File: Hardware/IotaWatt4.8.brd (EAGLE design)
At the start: 87 x 67.9 mm, 53 parts

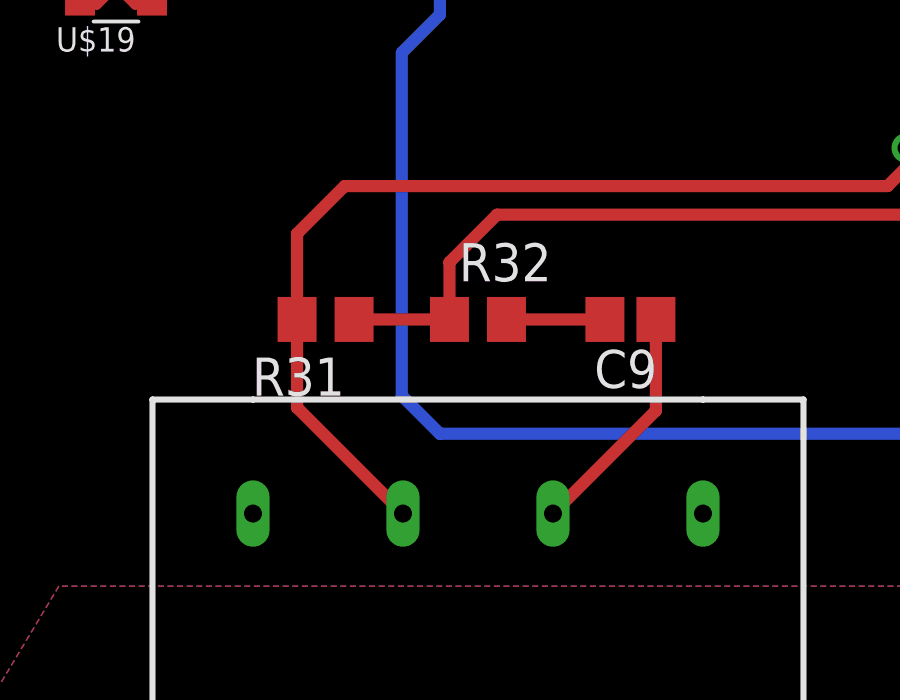
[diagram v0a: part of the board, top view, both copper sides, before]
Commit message: Revert "beginning to add a 2.2" TFT display"
This reverts commit 5a3055f75d7c66bfc0e3a1cc9d4d5180e17e1807.
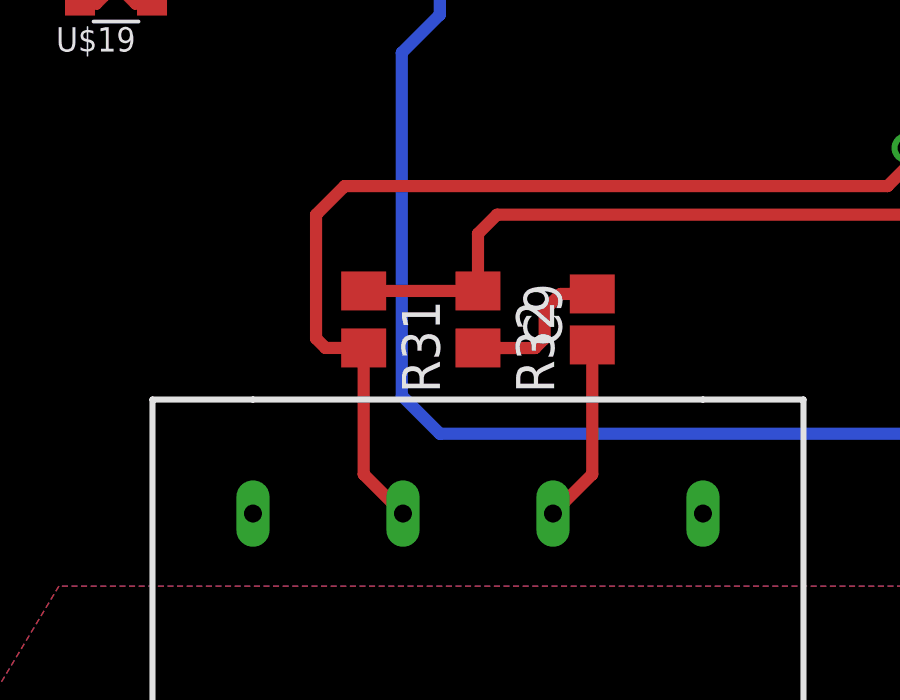
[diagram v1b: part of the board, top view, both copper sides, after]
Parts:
- moved C9 1.27 mm to (39.4, 34.3), turned to 90 degrees
- moved R31 1.27 mm to (31.8, 34.3), turned to 270 degrees
- turned R32 to 270 degrees
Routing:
- net N$17: track 3.28 -> 5.12 mm
- net N$27: track 7.89 -> 6.16 mm
- net ADC10: track 49.9 -> 49.2 mm
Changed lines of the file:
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@@
 <wire x1="17.78" y1="17.78" x2="63.5" y2="17.78" width="1.27" layer="46"/>
 <wire x1="10.16" y1="13.97" x2="16.51" y2="13.97" width="1.27" layer="46"/>
-<dimension x1="35.2425" y1="4.7625" x2="20.0025" y2="4.7625" x3="27.6225" y3="11.7475" textsize="1.778" layer="16"/>
 </plain>
 <attributes>
@@
 <attribute name="OC_NEWARK" value="unknown" x="20.0025" y="4.7625" size="1.778" layer="27" font="vector" display="off"/>
 </element>
-<element name="R31" library="resistor" package="R0805" value="1K" x="30.48" y="34.29" rot="R180"/>
-<element name="C9" library="adafruit" package="C0805" value="10uF" x="40.64" y="34.29" rot="R180"/>
-<element name="R32" library="resistor" package="R0805" value="12K" x="35.56" y="34.29"/>
+<element name="R31" library="resistor" package="R0805" value="1K" x="31.75" y="34.29" rot="R270"/>
+<element name="C9" library="adafruit" package="C0805" value="10uF" x="39.37" y="34.29" rot="R90"/>
+<element name="R32" library="resistor" package="R0805" value="12K" x="35.56" y="34.29" rot="R270"/>
 </elements>
 <signals>
@@
 <contactref element="R32" pad="1"/>
 <contactref element="R31" pad="1"/>
+<wire x1="31.75" y1="35.24" x2="35.56" y2="35.24" width="0.4064" layer="1"/>
+<wire x1="35.56" y1="35.24" x2="35.56" y2="37.1475" width="0.4064" layer="1"/>
+<wire x1="35.56" y1="37.1475" x2="36.195" y2="37.7825" width="0.4064" layer="1"/>
 <wire x1="36.195" y1="37.7825" x2="63.5" y2="37.7825" width="0.4064" layer="1"/>
 <wire x1="63.5" y1="37.7825" x2="64.77" y2="39.0525" width="0.4064" layer="1"/>
@@
 <wire x1="64.295" y1="50.68" x2="64.295" y2="48.1" width="0.4064" layer="1"/>
 <wire x1="64.295" y1="48.1" x2="64.4525" y2="47.9425" width="0.4064" layer="1"/>
-<wire x1="31.43" y1="34.29" x2="34.61" y2="34.29" width="0.4064" layer="1"/>
-<wire x1="36.195" y1="37.7825" x2="34.61" y2="36.1975" width="0.4064" layer="1"/>
-<wire x1="34.61" y1="36.1975" x2="34.61" y2="34.29" width="0.4064" layer="1"/>
 </signal>
 <signal name="GPIO16">
@@
 <contactref element="R31" pad="2"/>
 <contactref element="U$5" pad="6"/>
+<wire x1="33.06" y1="27.82" x2="31.75" y2="29.13" width="0.4064" layer="1"/>
+<wire x1="31.75" y1="29.13" x2="31.75" y2="33.34" width="0.4064" layer="1"/>
+<wire x1="31.75" y1="33.34" x2="30.4775" y2="33.34" width="0.4064" layer="1"/>
+<wire x1="30.4775" y1="33.34" x2="30.1625" y2="33.655" width="0.4064" layer="1"/>
+<wire x1="30.1625" y1="33.655" x2="30.1625" y2="37.7825" width="0.4064" layer="1"/>
+<wire x1="30.1625" y1="37.7825" x2="31.115" y2="38.735" width="0.4064" layer="1"/>
 <wire x1="31.115" y1="38.735" x2="49.2125" y2="38.735" width="0.4064" layer="1"/>
 <wire x1="49.2125" y1="38.735" x2="49.8475" y2="39.37" width="0.4064" layer="1"/>
@@
 <via x="49.8475" y="40.005" extent="1-16" drill="0.6" shape="octagon"/>
 <wire x1="49.8475" y1="48.26" x2="49.8475" y2="40.005" width="0.4064" layer="16"/>
-<wire x1="33.06" y1="27.82" x2="29.53" y2="31.35" width="0.4064" layer="1"/>
-<wire x1="29.53" y1="31.35" x2="29.53" y2="34.29" width="0.4064" layer="1"/>
-<wire x1="31.115" y1="38.735" x2="29.53" y2="37.15" width="0.4064" layer="1"/>
-<wire x1="29.53" y1="37.15" x2="29.53" y2="34.29" width="0.4064" layer="1"/>
 </signal>
 <signal name="N$7">
@@
 <contactref element="C9" pad="1"/>
 <contactref element="U$5" pad="7"/>
-<wire x1="38.06" y1="27.82" x2="41.49" y2="31.25" width="0.4064" layer="1"/>
-<wire x1="41.49" y1="31.25" x2="41.49" y2="34.29" width="0.4064" layer="1"/>
+<wire x1="38.06" y1="27.82" x2="39.37" y2="29.13" width="0.4064" layer="1"/>
+<wire x1="39.37" y1="29.13" x2="39.37" y2="33.44" width="0.4064" layer="1"/>
 </signal>
 <signal name="N$17">
 <contactref element="R32" pad="2"/>
 <contactref element="C9" pad="2"/>
-<wire x1="39.79" y1="34.29" x2="36.51" y2="34.29" width="0.4064" layer="1"/>
+<wire x1="39.37" y1="35.14" x2="38.315" y2="35.14" width="0.4064" layer="1"/>
+<wire x1="38.315" y1="35.14" x2="37.7825" y2="34.6075" width="0.4064" layer="1"/>
+<wire x1="37.7825" y1="34.6075" x2="37.7825" y2="33.655" width="0.4064" layer="1"/>
+<wire x1="37.7825" y1="33.655" x2="37.465" y2="33.3375" width="0.4064" layer="1"/>
+<wire x1="37.465" y1="33.3375" x2="35.5625" y2="33.3375" width="0.4064" layer="1"/>
+<wire x1="35.5625" y1="33.3375" x2="35.56" y2="33.34" width="0.4064" layer="1"/>
 </signal>
 </signals>
